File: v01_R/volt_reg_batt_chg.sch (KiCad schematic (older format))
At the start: 14 parts, among them P1 CONN_1, P2 CONN_1, Q3 PNP, U4 MIC5219

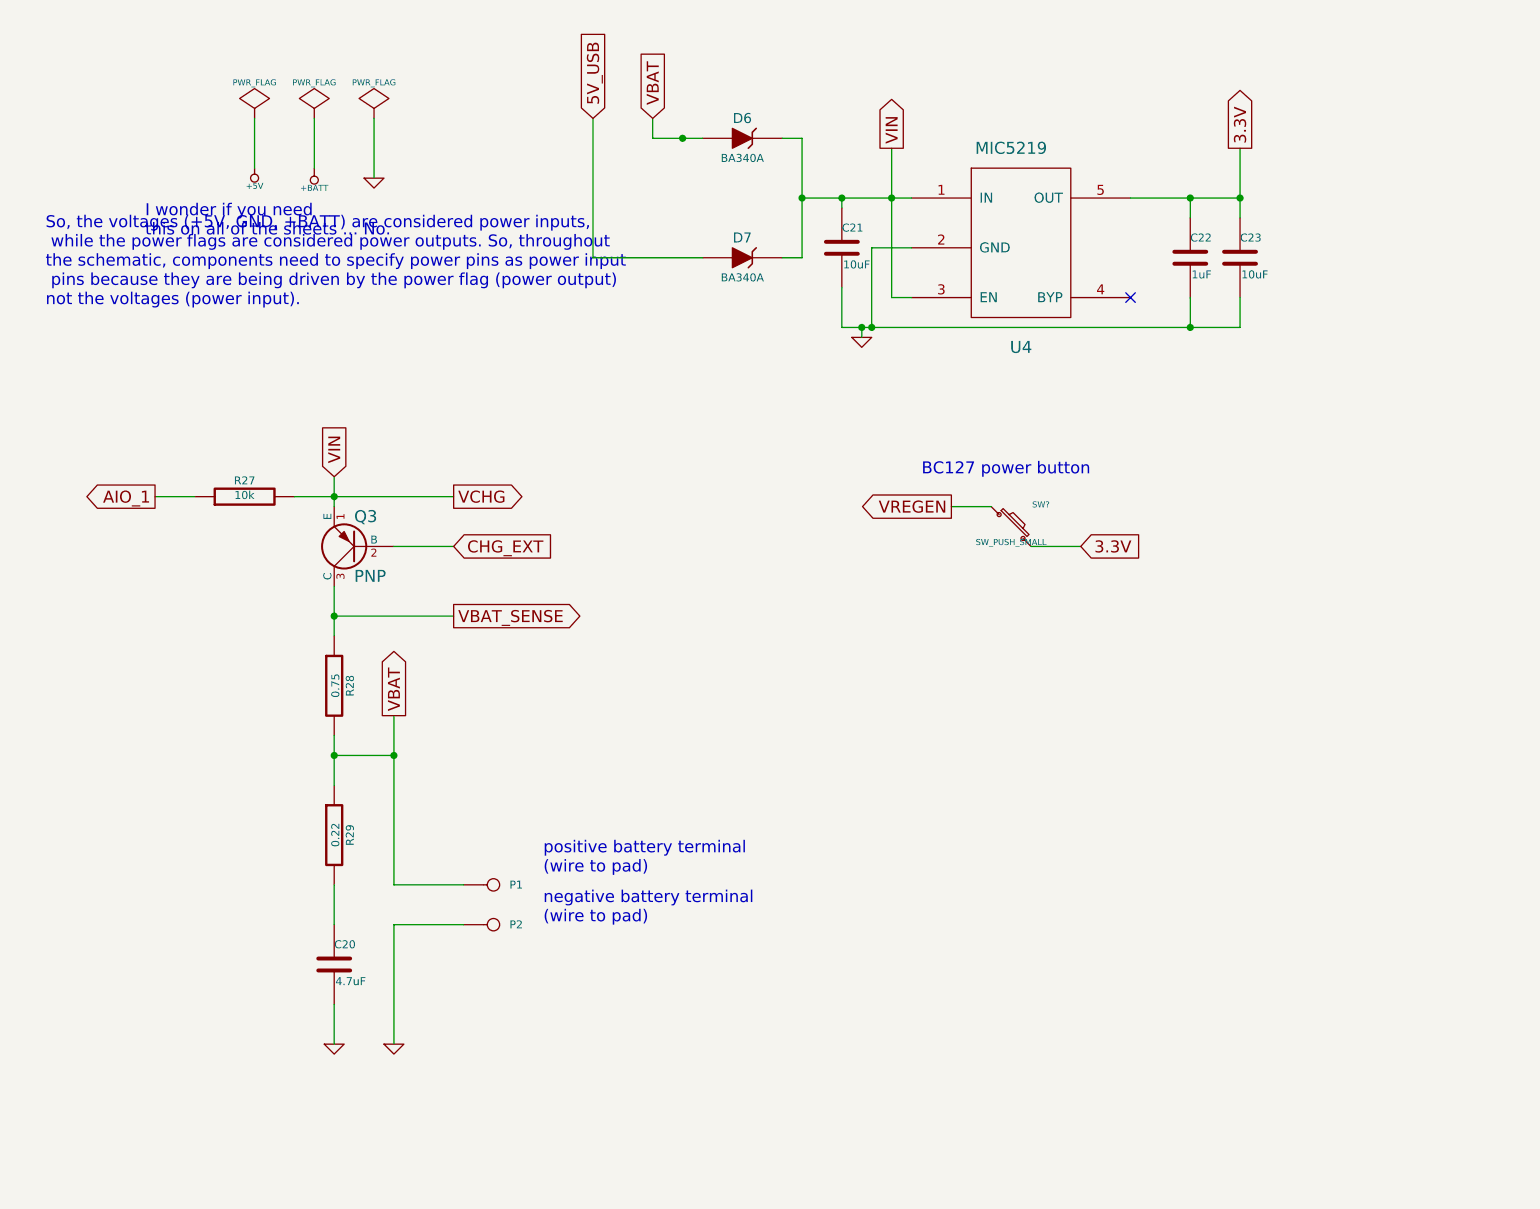
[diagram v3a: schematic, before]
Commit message: Update with 2.00" diameter version of the CWIEM R v01 PCB. The only change remaining was to finalize sound driver pad placement and sizing. After that, production files could be generated for board manufacturing.
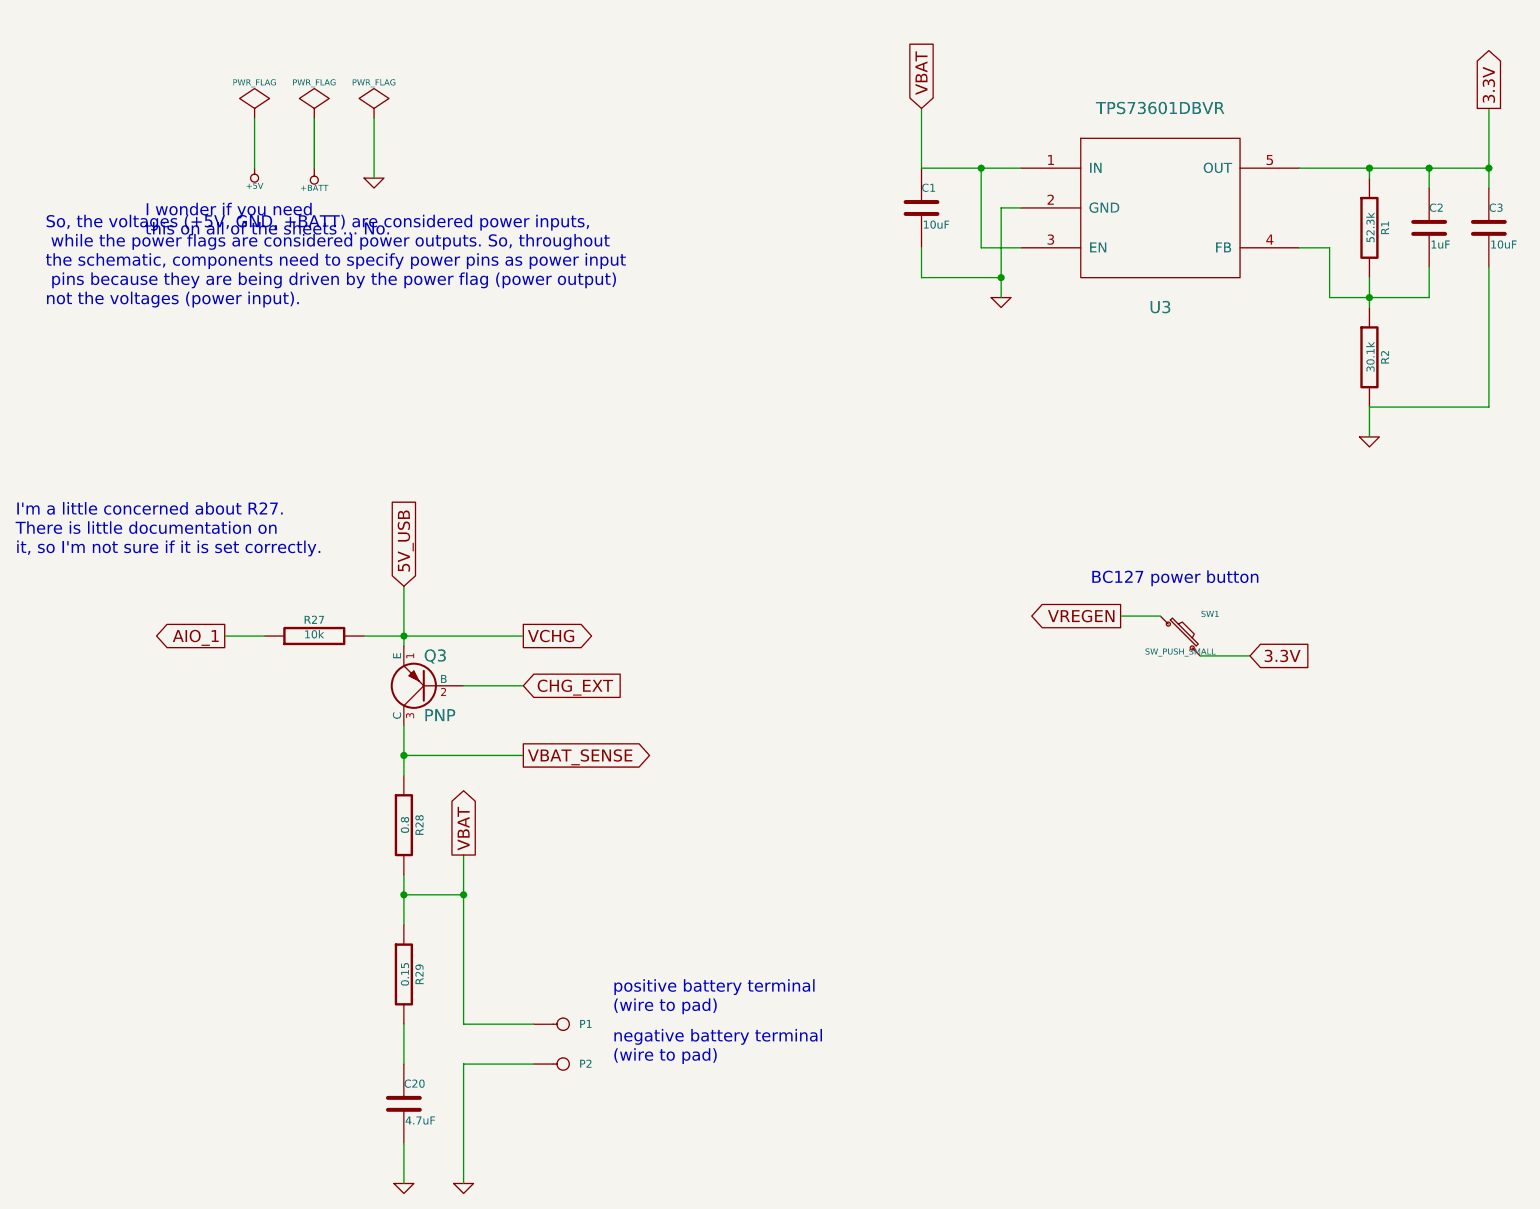
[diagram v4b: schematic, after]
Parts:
- removed C21, C23: 10uF, ~, symbol C
- removed C22: 1uF, ~, symbol C
- removed D6, D7: BA340A, ~, symbol ZENER
- removed U4: MIC5219, ~, symbol MIC5219
- added C1, C3: 10uF, ~, symbol C
- added C2: 1uF, ~, symbol C
- added R1: 52.3k, ~, symbol R
- added R2: 30.1k, ~, symbol R
- added U3: TPS73601DBVR, symbol TPS73601DBVR
- R28: value 0.75 -> 0.8
- R29: value 0.22 -> 0.15
- gave numbers to parts that had none: 1
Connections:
- net VCHG is gone; now on net 5V_USB: Q3.1 (E), R27.2
- net 3.3V: now also C2.1, C3.1, R1.1, U3.5 (OUT)
- net GND: now also C1.2, C3.2, R2.2, U3.2 (GND)
- net VBAT: now also C1.1, U3.1 (IN), U3.3 (EN)
- new net: C2.2, R1.2, R2.1, U3.4 (FB)
- no-connect marks 1 -> 0
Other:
- note added: "I'm a little concerned about R27. \nThere is little documentation on \nit, so I'm not sure if it is set correctly."
- moved on the sheet: C20, P1, P2, Q3, R27, R28, R29, SW1
